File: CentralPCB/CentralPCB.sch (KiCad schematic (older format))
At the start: 60 parts, among them J1 POWER HEADER, J2 INPUT HEADER, J3 SPI Header 0, J4 SPI Header 1, J5 MIDI-IN, J6 MIDI-OUT, U1 Teensy4.1

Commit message: Updated user interface pins
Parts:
- removed D2: WRN, symbol Device:LED
- removed D3: ERR, symbol Device:LED
- removed D4: COM, symbol Device:LED
- removed D? (x15): 12v Zener, Diode_SMD:D_SOD-123, symbol Diode:BZT52Bxx
- removed J2: INPUT HEADER, RJHSE508004, symbol RJHSE-5080-04:RJHSE-5080-04
- removed J3: SPI Header 0, symbol Connector_Generic:Conn_01x04
- removed J5: MIDI-IN, DIN5-RA-PTH, symbol SparkFun-KiCad-Libraries-master_Libraries_SparkFun-Connectors:DIN5
- removed J6: MIDI-OUT, DIN5-RA-PTH, symbol SparkFun-KiCad-Libraries-master_Libraries_SparkFun-Connectors:DIN5
- removed R? (x16): 3.3kOhm, symbol Device:R_US
- removed R? (x16): 6.65kOhm, symbol Device:R_US
- added D19, D21, D22: POW, LED_THT:LED_D3.0mm, symbol Device:LED
- added D20: 12V_POW, LED_THT:LED_D3.0mm, symbol Device:LED
- added D5: 5V_POW, LED_THT:LED_D3.0mm, symbol Device:LED
- added D? (x15): 4.3v Zener, Diode_SMD:D_SOD-123, symbol Diode:BZT52Bxx
- added J5: MIDI IN, Connector_PinSocket_2.54mm:PinSocket_1x03_P2.54mm_Vertical, symbol Connector_Generic:Conn_01x03
- added J6: MIDI OUT, Connector_PinSocket_2.54mm:PinSocket_1x03_P2.54mm_Vertical, symbol Connector_Generic:Conn_01x03
- added J?: Conn_02x16_Top_Bottom, Connector_PinSocket_2.54mm:PinSocket_2x16_P2.54mm_Vertical, symbol Connector_Generic:Conn_02x16_Top_Bottom
- added J?: Conn_01x05, symbol Connector_Generic:Conn_01x05
- added R33, R34, R35, R36, R37, R38: ?, Resistor_SMD:R_0805_2012Metric, symbol Device:R_US
- added TH1, TH2, TH3: Thermistor_US, Resistor_SMD:R_1206_3216Metric, symbol Device:Thermistor_US
- D1: footprint (none) -> LED_THT:LED_D3.0mm
- D2: renamed from D?; value 12v Zener -> 4.3v Zener
- J1: footprint (none) -> Connector_PinSocket_2.54mm:PinSocket_2x08_P2.54mm_Vertical
- J4: footprint (none) -> Connector_PinSocket_2.54mm:PinSocket_1x04_P2.54mm_Vertical
- gave numbers to parts that had none: 1
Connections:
- net labels added: +3.3V, MIDREC
- wire segments 236 -> 219
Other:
- moved on the sheet: D1, D2, J1, J4, U2

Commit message: Fixed diodes
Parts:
- removed D2, D? (x14): 4.3v Zener, Diode_SMD:D_SOD-123, symbol Diode:BZT52Bxx
- added D? (x15): 3.3v Zener, Diode_SMD:D_SOD-123, symbol Diode:BZT52Bxx
- D?: value 4.3v Zener -> 3.3v Zener
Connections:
- wire segments 219 -> 218
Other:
- moved on the sheet: D?

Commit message: PCB update
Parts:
- removed J?: Conn_02x16_Top_Bottom, Connector_PinSocket_2.54mm:PinSocket_2x16_P2.54mm_Vertical, symbol Connector_Generic:Conn_02x16_Top_Bottom
- added J3: Conn_02x16_Odd_Even, Connector_PinSocket_2.54mm:PinSocket_2x16_P2.54mm_Vertical, symbol Connector_Generic:Conn_02x16_Odd_Even
- added R10, R11, R12, R13, R14, R15, R16, R17, R18, R19, R20, R21, R22, R7, R8, R9: 200, Resistor_SMD:R_0805_2012Metric, symbol Device:R_US
- added U1: AD8531, Package_SO:SOIC-8_3.9x4.9mm_P1.27mm, symbol Amplifier_Operational:OP179GS
- J2: renamed from J4; value SPI Header 1 -> SPI Header
- J6: renamed from J?; value Conn_01x05 -> DAC Comm; footprint (none) -> Connector_PinSocket_2.54mm:PinSocket_1x05_P2.54mm_Vertical
- U2: renamed from U1; footprint (none) -> teensy:Teensy41
- gave numbers to parts that had none: 16
- renumbered D5 to D1, D20 to D2, D1 to D3, D19 to D4, D21 to D5, D22 to D6, J5 to J4, J6 to J5, R33 to R1, R34 to R2, R35 to R3, R36 to R4, R37 to R5, R38 to R6, U2 to U3
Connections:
- wire segments 218 -> 241
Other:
- moved on the sheet: D1, D10, D11, D12, D13, D14, D15, D16, D17, D18, D19, D2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

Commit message: Fixed Teensy connections
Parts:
- removed J4: MIDI IN, Connector_PinSocket_2.54mm:PinSocket_1x03_P2.54mm_Vertical, symbol Connector_Generic:Conn_01x03
- removed J5: MIDI OUT, Connector_PinSocket_2.54mm:PinSocket_1x03_P2.54mm_Vertical, symbol Connector_Generic:Conn_01x03
- renumbered J6 to J4
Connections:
- wire segments 241 -> 227

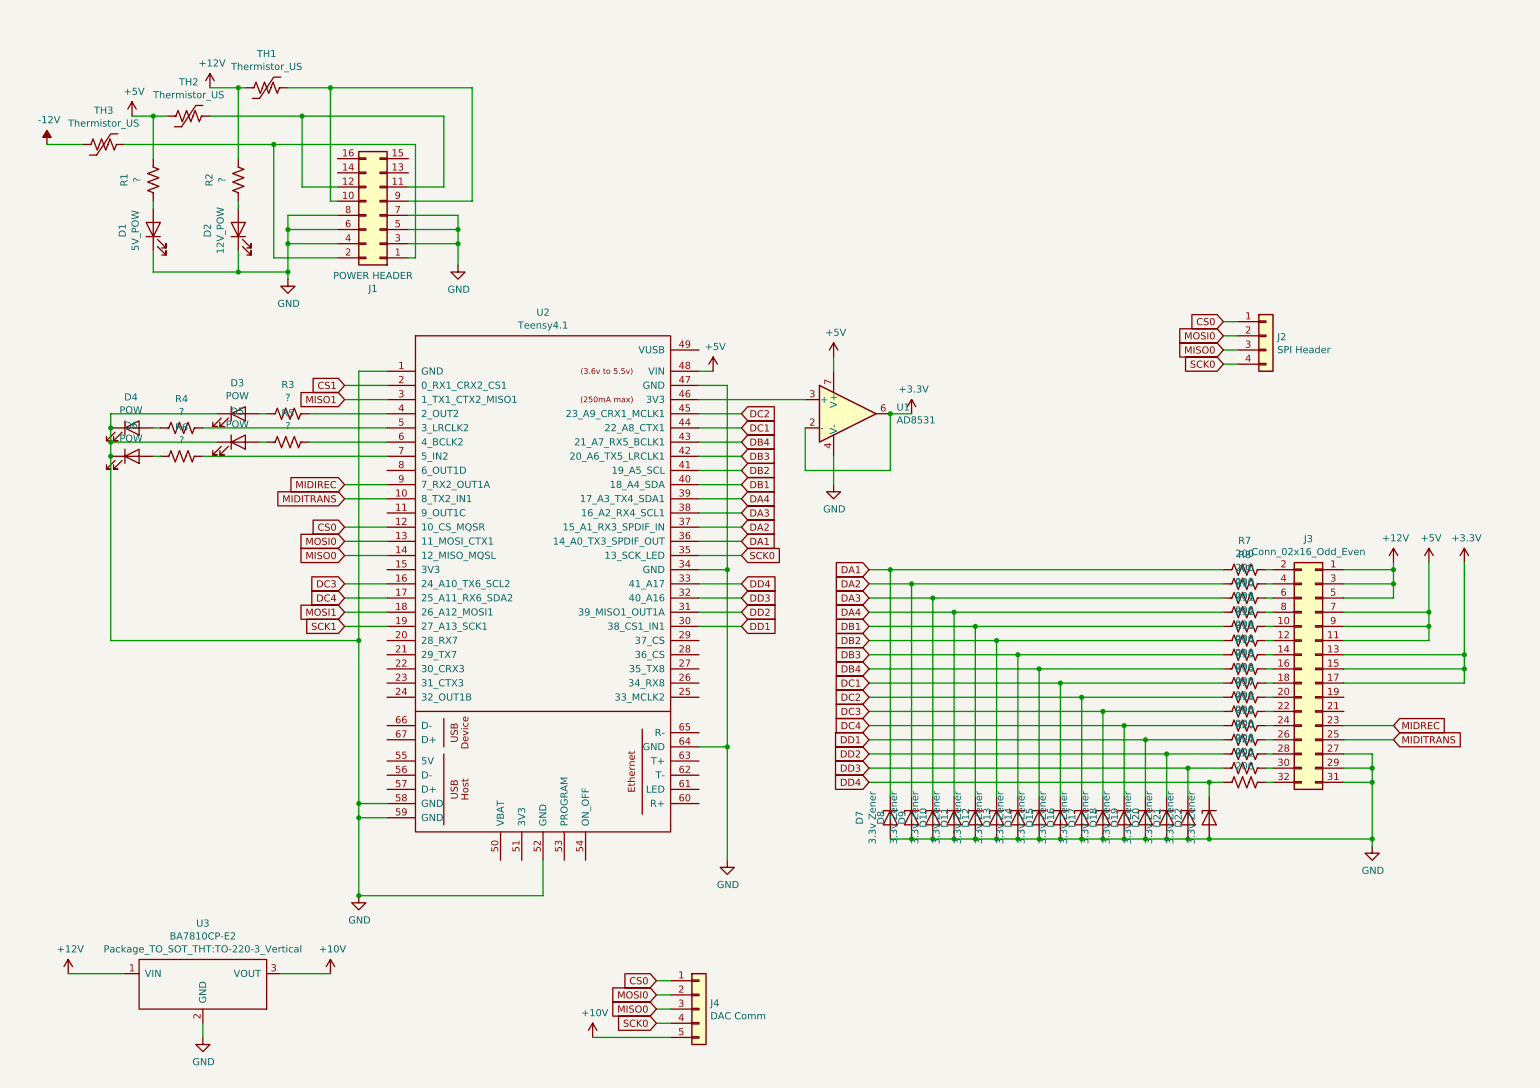
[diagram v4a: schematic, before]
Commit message: Consolidated pin headers
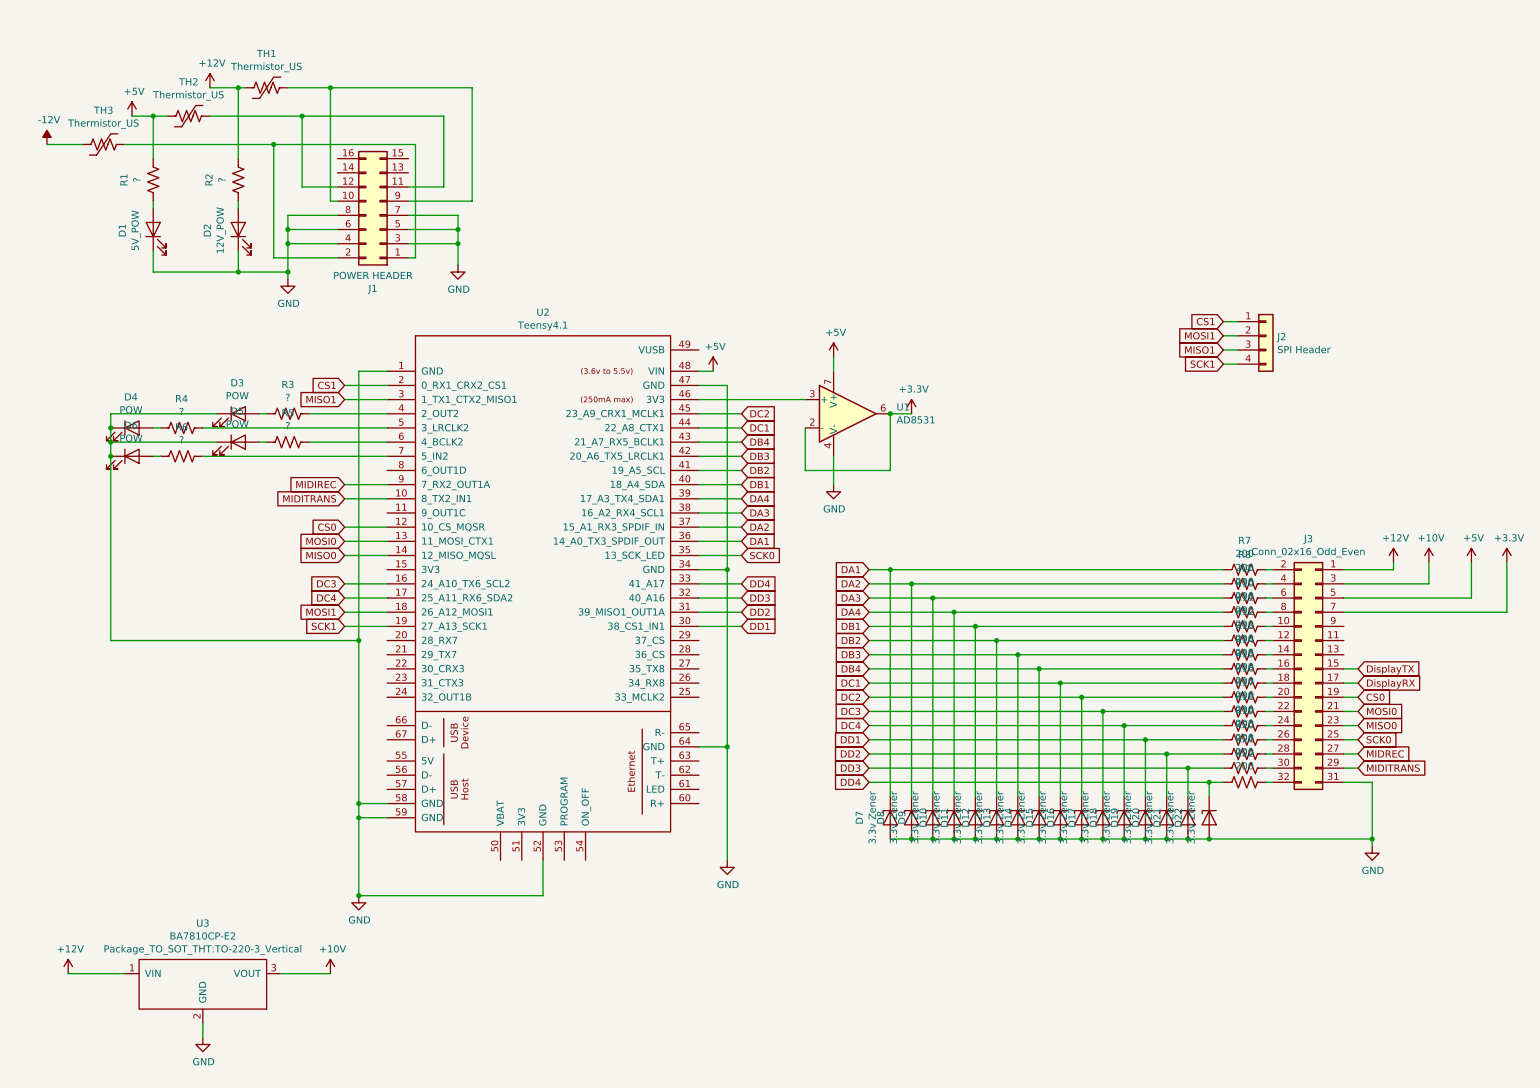
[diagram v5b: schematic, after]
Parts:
- removed J4: DAC Comm, Connector_PinSocket_2.54mm:PinSocket_1x05_P2.54mm_Vertical, symbol Connector_Generic:Conn_01x05
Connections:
- net +10V: now also J3.3 (Pin_3)
- net +12V: no longer J3.3 (Pin_3), J3.5 (Pin_5)
- net +3V3: now also J3.7 (Pin_7); no longer J3.13 (Pin_13), J3.15 (Pin_15), J3.17 (Pin_17)
- net +5V: now also J3.5 (Pin_5); no longer J3.11 (Pin_11), J3.7 (Pin_7), J3.9 (Pin_9)
- net CS0: now also J3.19 (Pin_19); no longer J2.1 (Pin_1)
- net CS1: now also J2.1 (Pin_1)
- net GND: no longer J3.27 (Pin_27), J3.29 (Pin_29)
- net MIDITRANS: now also J3.29 (Pin_29); no longer J3.25 (Pin_25)
- net MIDREC: now also J3.27 (Pin_27); no longer J3.23 (Pin_23)
- net MISO0: now also J3.23 (Pin_23); no longer J2.3 (Pin_3)
- net MISO1: now also J2.3 (Pin_3)
- net MOSI0: now also J3.21 (Pin_21); no longer J2.2 (Pin_2)
- net MOSI1: now also J2.2 (Pin_2)
- net SCK0: now also J3.25 (Pin_25); no longer J2.4 (Pin_4)
- net SCK1: now also J2.4 (Pin_4)
- new net DisplayRX: J3.17 (Pin_17)
- new net DisplayTX: J3.15 (Pin_15)
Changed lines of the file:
@@
 $EndComp
 $Comp
-L power:GND #PWR014
+L power:GND #PWR015
 U 1 1 616B52F2
 P 5500 6250
-F 0 "#PWR014" H 5500 6000 50  0001 C CNN
+F 0 "#PWR015" H 5500 6000 50  0001 C CNN
 F 1 "GND" H 5505 6077 50  0000 C CNN
 F 2 "" H 5500 6250 50  0001 C CNN
@@
 $EndComp
 $Comp
-L power:GND #PWR015
+L power:GND #PWR016
 U 1 1 616B5948
 P 2900 6500
-F 0 "#PWR015" H 2900 6250 50  0001 C CNN
+F 0 "#PWR016" H 2900 6250 50  0001 C CNN
 F 1 "GND" H 2905 6327 50  0000 C CNN
 F 2 "" H 2900 6500 50  0001 C CNN
@@
 $EndComp
 $Comp
-L power:+12V #PWR016
+L power:+12V #PWR017
 U 1 1 61611891
 P 850 7050
-F 0 "#PWR016" H 850 6900 50  0001 C CNN
+F 0 "#PWR017" H 850 6900 50  0001 C CNN
 F 1 "+12V" H 865 7223 50  0000 C CNN
 F 2 "" H 850 7050 50  0001 C CNN
@@
 $EndComp
 $Comp
-L power:GND #PWR018
+L power:GND #PWR019
 U 1 1 616148AD
 P 1800 7500
-F 0 "#PWR018" H 1800 7250 50  0001 C CNN
+F 0 "#PWR019" H 1800 7250 50  0001 C CNN
 F 1 "GND" H 1805 7327 50  0000 C CNN
 F 2 "" H 1800 7500 50  0001 C CNN
@@
 $EndComp
 $Comp
-L power:+10V #PWR017
+L power:+10V #PWR018
 U 1 1 61617614
 P 2700 7050
-F 0 "#PWR017" H 2700 6900 50  0001 C CNN
+F 0 "#PWR018" H 2700 6900 50  0001 C CNN
 F 1 "+10V" H 2715 7223 50  0000 C CNN
 F 2 "" H 2700 7050 50  0001 C CNN
@@
 Text GLabel 5600 4100 2    50   Input ~ 0
 SCK0
-Text GLabel 5000 7200 0    50   Input ~ 0
-MOSI0
-Text GLabel 5000 7300 0    50   Input ~ 0
-MISO0
-Text GLabel 5000 7400 0    50   Input ~ 0
-SCK0
 Text GLabel 2800 3900 0    50   Input ~ 0
-CS0
-Text GLabel 5000 7100 0    50   Input ~ 0
 CS0
 Text GLabel 5600 3900 2    50   Input ~ 0
@@
 DD4
 Text GLabel 9000 2550 0    50   Input ~ 0
-MOSI0
+MOSI1
 Text GLabel 9000 2650 0    50   Input ~ 0
-MISO0
+MISO1
 Text GLabel 9000 2750 0    50   Input ~ 0
-SCK0
+SCK1
 $Comp
 L Connector_Generic:Conn_01x04 J2
@@
 $EndComp
 Text GLabel 9000 2450 0    50   Input ~ 0
-CS0
+CS1
 Text GLabel 2800 4500 0    50   Input ~ 0
 MOSI1
@@
 L power:+3.3V #PWR012
 U 1 1 623E2584
-P 10700 4150
-F 0 "#PWR012" H 10700 4000 50  0001 C CNN
-F 1 "+3.3V" H 10715 4323 50  0000 C CNN
-F 2 "" H 10700 4150 50  0001 C CNN
-F 3 "" H 10700 4150 50  0001 C CNN
-	1    10700 4150
-	1    0    0    -1
-$EndComp
-$Comp
-L Connector_Generic:Conn_01x05 J4
-U 1 1 626A8EDE
-P 5300 7300
-F 0 "J4" H 5380 7342 50  0000 L CNN
-F 1 "DAC Comm" H 5380 7251 50  0000 L CNN
-F 2 "Connector_PinSocket_2.54mm:PinSocket_1x05_P2.54mm_Vertical" H 5300 7300 50  0001 C CNN
-F 3 "~" H 5300 7300 50  0001 C CNN
-	1    5300 7300
-	1    0    0    -1
-$EndComp
-$Comp
-L power:+10V #PWR019
+P 11000 4150
+F 0 "#PWR012" H 11000 4000 50  0001 C CNN
+F 1 "+3.3V" H 11015 4323 50  0000 C CNN
+F 2 "" H 11000 4150 50  0001 C CNN
+F 3 "" H 11000 4150 50  0001 C CNN
+	1    11000 4150
+	1    0    0    -1
+$EndComp
+$Comp
+L power:+10V #PWR013
 U 1 1 626A98C8
-P 4550 7500
-F 0 "#PWR019" H 4550 7350 50  0001 C CNN
-F 1 "+10V" H 4565 7673 50  0000 C CNN
-F 2 "" H 4550 7500 50  0001 C CNN
-F 3 "" H 4550 7500 50  0001 C CNN
-	1    4550 7500
+P 10450 4150
+F 0 "#PWR013" H 10450 4000 50  0001 C CNN
+F 1 "+10V" H 10465 4323 50  0000 C CNN
+F 2 "" H 10450 4150 50  0001 C CNN
+F 3 "" H 10450 4150 50  0001 C CNN
+	1    10450 4150
 	1    0    0    -1
 $EndComp
@@
 L power:+5V #PWR011
 U 1 1 618C6CC3
-P 10450 4150
-F 0 "#PWR011" H 10450 4000 50  0001 C CNN
-F 1 "+5V" H 10465 4323 50  0000 C CNN
-F 2 "" H 10450 4150 50  0001 C CNN
-F 3 "" H 10450 4150 50  0001 C CNN
-	1    10450 4150
+P 10750 4150
+F 0 "#PWR011" H 10750 4000 50  0001 C CNN
+F 1 "+5V" H 10765 4323 50  0000 C CNN
+F 2 "" H 10750 4150 50  0001 C CNN
+F 3 "" H 10750 4150 50  0001 C CNN
+	1    10750 4150
 	1    0    0    -1
 $EndComp
@@
 $EndComp
 $Comp
-L power:GND #PWR013
+L power:GND #PWR014
 U 1 1 6161C083
 P 10050 6150
-F 0 "#PWR013" H 10050 5900 50  0001 C CNN
+F 0 "#PWR014" H 10050 5900 50  0001 C CNN
 F 1 "GND" H 10055 5977 50  0000 C CNN
 F 2 "" H 10050 6150 50  0001 C CNN
@@
 	1    0    0    -1
 $EndComp
-Text GLabel 10200 5300 2    50   Input ~ 0
+Text GLabel 9950 5500 2    50   Input ~ 0
 MIDREC
-Text GLabel 10200 5400 2    50   Input ~ 0
+Text GLabel 9950 5600 2    50   Input ~ 0
 MIDITRANS
 $Comp
@@
 	3100 5850 2900 5850
 Wire Wire Line
-	3100 3700 2800 3700
-Connection ~ 10050 5600
-Wire Wire Line
-	10050 5500 10050 5600
-Wire Wire Line
-	9850 5500 10050 5500
-Wire Wire Line
-	9850 5400 10200 5400
-Wire Wire Line
 	5500 4200 5500 5450
 Wire Wire Line
@@
 Wire Wire Line
 	5500 5450 5500 6250
-Wire Wire Line
-	9850 5300 10200 5300
-Connection ~ 10700 4900
-Wire Wire Line
-	10700 5000 10700 4900
-Wire Wire Line
-	9850 5000 10700 5000
-Wire Wire Line
-	10700 4800 10700 4900
-Connection ~ 10700 4800
-Wire Wire Line
-	10700 4150 10700 4800
-Wire Wire Line
-	9850 4900 10700 4900
-Wire Wire Line
-	9850 4800 10700 4800
-Connection ~ 10450 4600
-Wire Wire Line
-	10450 4700 10450 4600
-Wire Wire Line
-	9850 4700 10450 4700
-Connection ~ 10450 4500
-Wire Wire Line
-	10450 4600 10450 4500
-Wire Wire Line
-	9850 4600 10450 4600
-Wire Wire Line
-	10450 4500 10450 4150
-Wire Wire Line
-	9850 4500 10450 4500
-Wire Wire Line
-	10200 4200 10200 4300
-Connection ~ 10200 4200
-Wire Wire Line
-	9850 4200 10200 4200
-Wire Wire Line
-	10200 4300 10200 4400
-Connection ~ 10200 4300
-Wire Wire Line
-	10200 4150 10200 4200
-Wire Wire Line
-	9850 4300 10200 4300
-Wire Wire Line
-	9850 4400 10200 4400
-Connection ~ 10050 5700
-Wire Wire Line
-	10050 5600 10050 5700
-Wire Wire Line
-	9850 5600 10050 5600
 Wire Wire Line
 	8900 5700 9000 5700
@@
 Wire Wire Line
 	9850 5700 10050 5700
-Wire Wire Line
-	4550 7500 5100 7500
 Connection ~ 1150 3200
 Connection ~ 1150 3300
@@
 	1450 3200 1500 3200
 Wire Wire Line
-	3100 3600 2800 3600
-Wire Wire Line
 	3100 4600 2800 4600
 Wire Wire Line
@@
 Wire Wire Line
 	9100 2450 9000 2450
-Wire Wire Line
-	5000 7400 5100 7400
-Wire Wire Line
-	5000 7300 5100 7300
-Wire Wire Line
-	5000 7200 5100 7200
-Wire Wire Line
-	5100 7100 5000 7100
 Wire Wire Line
 	850  7050 1250 7050
@@
 	1    0    0    -1
 $EndComp
+Text GLabel 9950 5200 2    50   Input ~ 0
+MOSI0
+Text GLabel 9950 5300 2    50   Input ~ 0
+MISO0
+Text GLabel 9950 5400 2    50   Input ~ 0
+SCK0
+Text GLabel 9950 5100 2    50   Input ~ 0
+CS0
+Text GLabel 9950 4900 2    50   Input ~ 0
+DisplayTX
+Text GLabel 9950 5000 2    50   Input ~ 0
+DisplayRX
+Wire Wire Line
+	9950 5600 9850 5600
+Wire Wire Line
+	9850 5500 9950 5500
+Wire Wire Line
+	9950 5400 9850 5400
+Wire Wire Line
+	9850 5300 9950 5300
+Wire Wire Line
+	9950 5200 9850 5200
+Wire Wire Line
+	9850 5100 9950 5100
+Wire Wire Line
+	9950 5000 9850 5000
+Wire Wire Line
+	9850 4900 9950 4900
+Wire Wire Line
+	9850 4200 10200 4200
+Wire Wire Line
+	10200 4200 10200 4150
+Wire Wire Line
+	9850 4300 10450 4300
+Wire Wire Line
+	10450 4300 10450 4150
+Wire Wire Line
+	9850 4400 10750 4400
+Wire Wire Line
+	10750 4400 10750 4150
+Wire Wire Line
+	9850 4500 11000 4500
+Wire Wire Line
+	11000 4500 11000 4150
+Wire Wire Line
+	3100 3600 2800 3600
+Wire Wire Line
+	2800 3700 3100 3700
 $EndSCHEMATC
